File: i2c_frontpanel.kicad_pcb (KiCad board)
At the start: 2 copper layers, 90 parts, among them CON1 AVR-ISP-6-DR, IC1 ATTINY88-A, Q1 2N7002, Q2 2N7002, Q3 2N7002, Q4 2N7002, Q5 2N7002, Q6 2N7002, U1 74HC14D_653, U10 MC14543B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

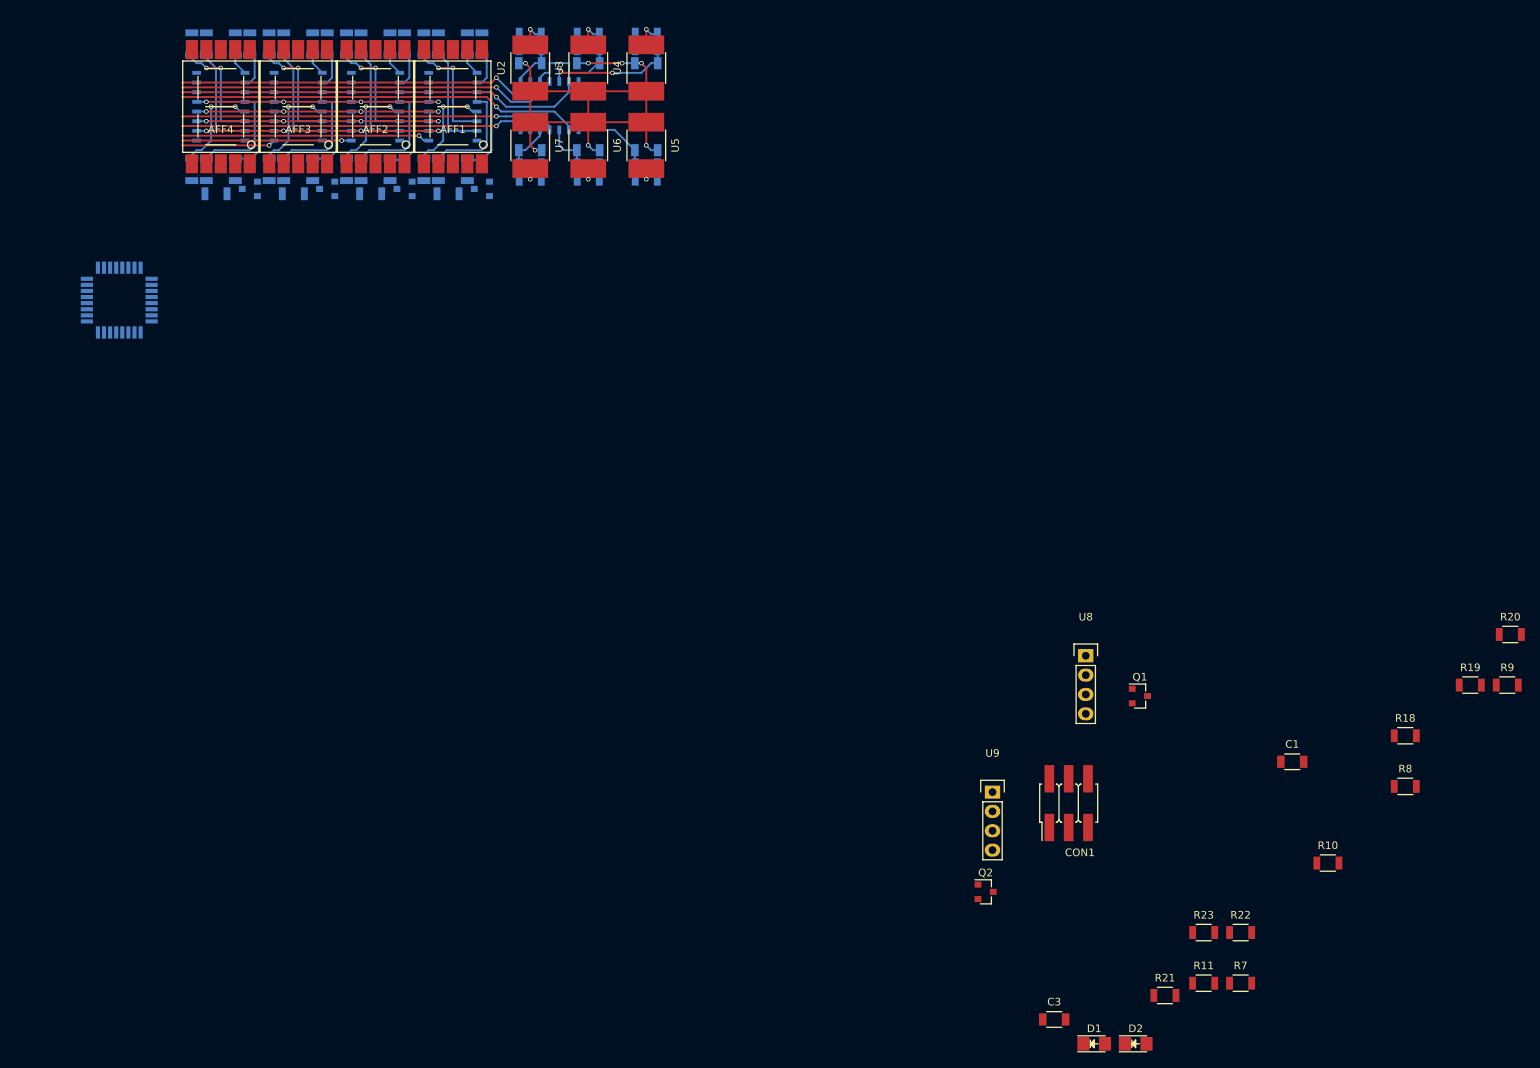
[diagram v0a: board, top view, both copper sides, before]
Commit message: PCB routing done.
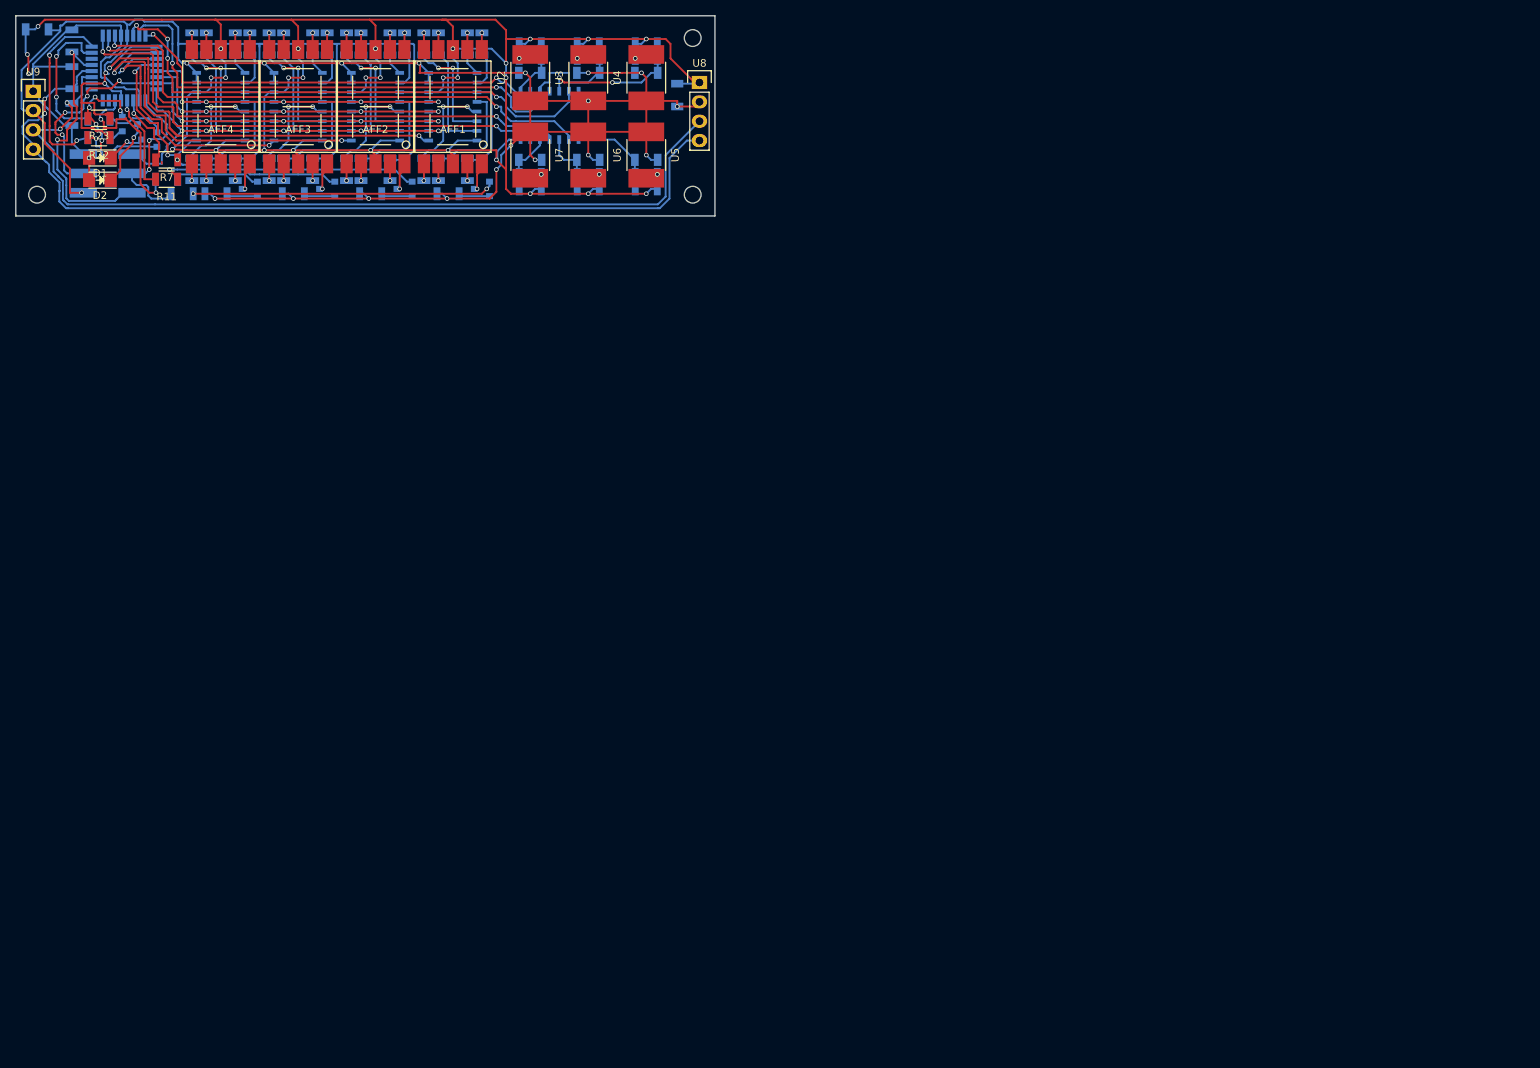
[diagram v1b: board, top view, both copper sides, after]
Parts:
- added ?: M2, Mounting_Holes:MountingHole_2.2mm_M2, F.Cu at (35.6, 44.6)
- added ?: M2, Mounting_Holes:MountingHole_2.2mm_M2, F.Cu at (121.7, 24.0)
- added ?: M2, Mounting_Holes:MountingHole_2.2mm_M2, F.Cu at (121.7, 44.6)
- C1, C3, Q1, Q2, R10, R18, R19, R20, R21, R8, R9: moved to B.Cu
- CON1: value AVR-ISP-6-DR -> AVR-ISP; moved to B.Cu
- U8: value I2C_4PINS -> SCL SCA GND Vcc
- U9: value I2C_4PINS -> SCL SDA GND Vcc
- moved R9 206.6 mm to (40.1, 24.4), turned to 270 degrees
- moved R20 200.9 mm to (40.1, 34.0), turned to 90 degrees
- moved R19 193.9 mm to (43.7, 37.1), turned to 180 degrees
- moved C1 190.9 mm to (35.6, 22.9)
- moved R18 189.7 mm to (43.7, 34.7), turned to 180 degrees
- moved R21 187.4 mm to (40.1, 29.2), turned to 270 degrees
- moved R22 182.7 mm to (43.7, 37.1), turned to 180 degrees
- moved R8 181.2 mm to (52.6, 42.5), turned to 180 degrees
- moved R23 180.2 mm to (43.7, 34.5), turned to 180 degrees
- moved R7 177.7 mm to (52.6, 40.0), turned to 180 degrees
- moved D2 177.1 mm to (43.8, 42.7), turned to 180 degrees
- moved D1 174.9 mm to (43.8, 39.8), turned to 180 degrees
- moved R10 174.3 mm to (54.6, 44.5), turned to 180 degrees
- moved R11 172.3 mm to (52.6, 42.5), turned to 180 degrees
- moved U9 156.0 mm to (35.1, 31.0)
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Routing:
- net VCC: track 0.00 -> 363.6 mm, vias 0 -> 31
- net GND: track 74.3 -> 324.5 mm, vias 7 -> 21
- net /SCL: track 0.00 -> 117.0 mm, vias 0 -> 2
- net /SDA: track 0.00 -> 116.6 mm, vias 0 -> 2
- net /DP0: track 0.00 -> 39.9 mm, vias 0 -> 2
- net /B: track 35.6 -> 73.1 mm, vias 4 -> 9
- net /RST: track 0.00 -> 34.6 mm, vias 0 -> 2
- net /DP1: track 0.00 -> 32.1 mm, vias 0 -> 1
- net /LD0: track 32.6 -> 60.2 mm, vias 1 -> 2
- net /LD1: track 22.2 -> 47.8 mm, vias 1 -> 2
- net /LED2: track 0.00 -> 24.4 mm, vias 0 -> 2
- net /DP2: track 0.00 -> 24.1 mm, vias 0 -> 1
- net Net-(IC1-Pad22): track 0.00 -> 23.3 mm, vias 0 -> 2
- net /SCK: track 0.00 -> 23.2 mm, vias 0 -> 2
- net /LD2: track 12.3 -> 35.2 mm, vias 1 -> 2
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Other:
- board outline added: 91.8 x 26.3 mm
